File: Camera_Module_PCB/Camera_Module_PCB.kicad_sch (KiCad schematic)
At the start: 66 parts, among them J3 FFC2A32-24-T, SW2 SW_Push, SW3 SW_Push, U2 ESP32-S3R8, U4 MAX98357AETE_T, U5 AP3032KTR-G1, Y1 40MHz

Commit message: Made minor changes to schematic
Schematic is finished except for the inclusion of an RF antenna for Pin 1 of the ESP32. Waiting on team confirmation about its inclusion.
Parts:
- added TP1, TP2, TP3, TP4, TP5, TP6: TestPoint, symbol Connector:TestPoint
- R17: value Riset -> 10
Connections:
- net IR_DIM is gone; now on net LED_CT: U2.37 (SPICLK_P)
- net +3.3V: now also TP4.1
- net GND: now also TP3.1
- net LED_CT: no longer U2.38 (GPIO33)
- net XTAL_N: now also TP6.1
- net at C14.2, L2.1, Y1.1: now also TP5.1
- net at D20.2, U2.50 (U0RXD), U3.3: now also TP2.1; no longer D19.2
- net at U2.49 (U0TXD), U3.4: now also D19.2, TP1.1
- no-connect marks 11 -> 20
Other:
- sheet Power Supply ports: added USB_D+, USB_D-; removed none
- note added: "CAMERA FFC CONNECTOR"
- note added: "LED DRIVER"
- note added: "Place close to VDD CPU & VDD RTC on ESP32"
- note added: "Place close toVDDA1 & 2 on ESP32"
- note removed: "Camera Connector"
- moved on the sheet: C27, C28, C32, C33, C7, C9, D19, D20, D21, D22, D23, J3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

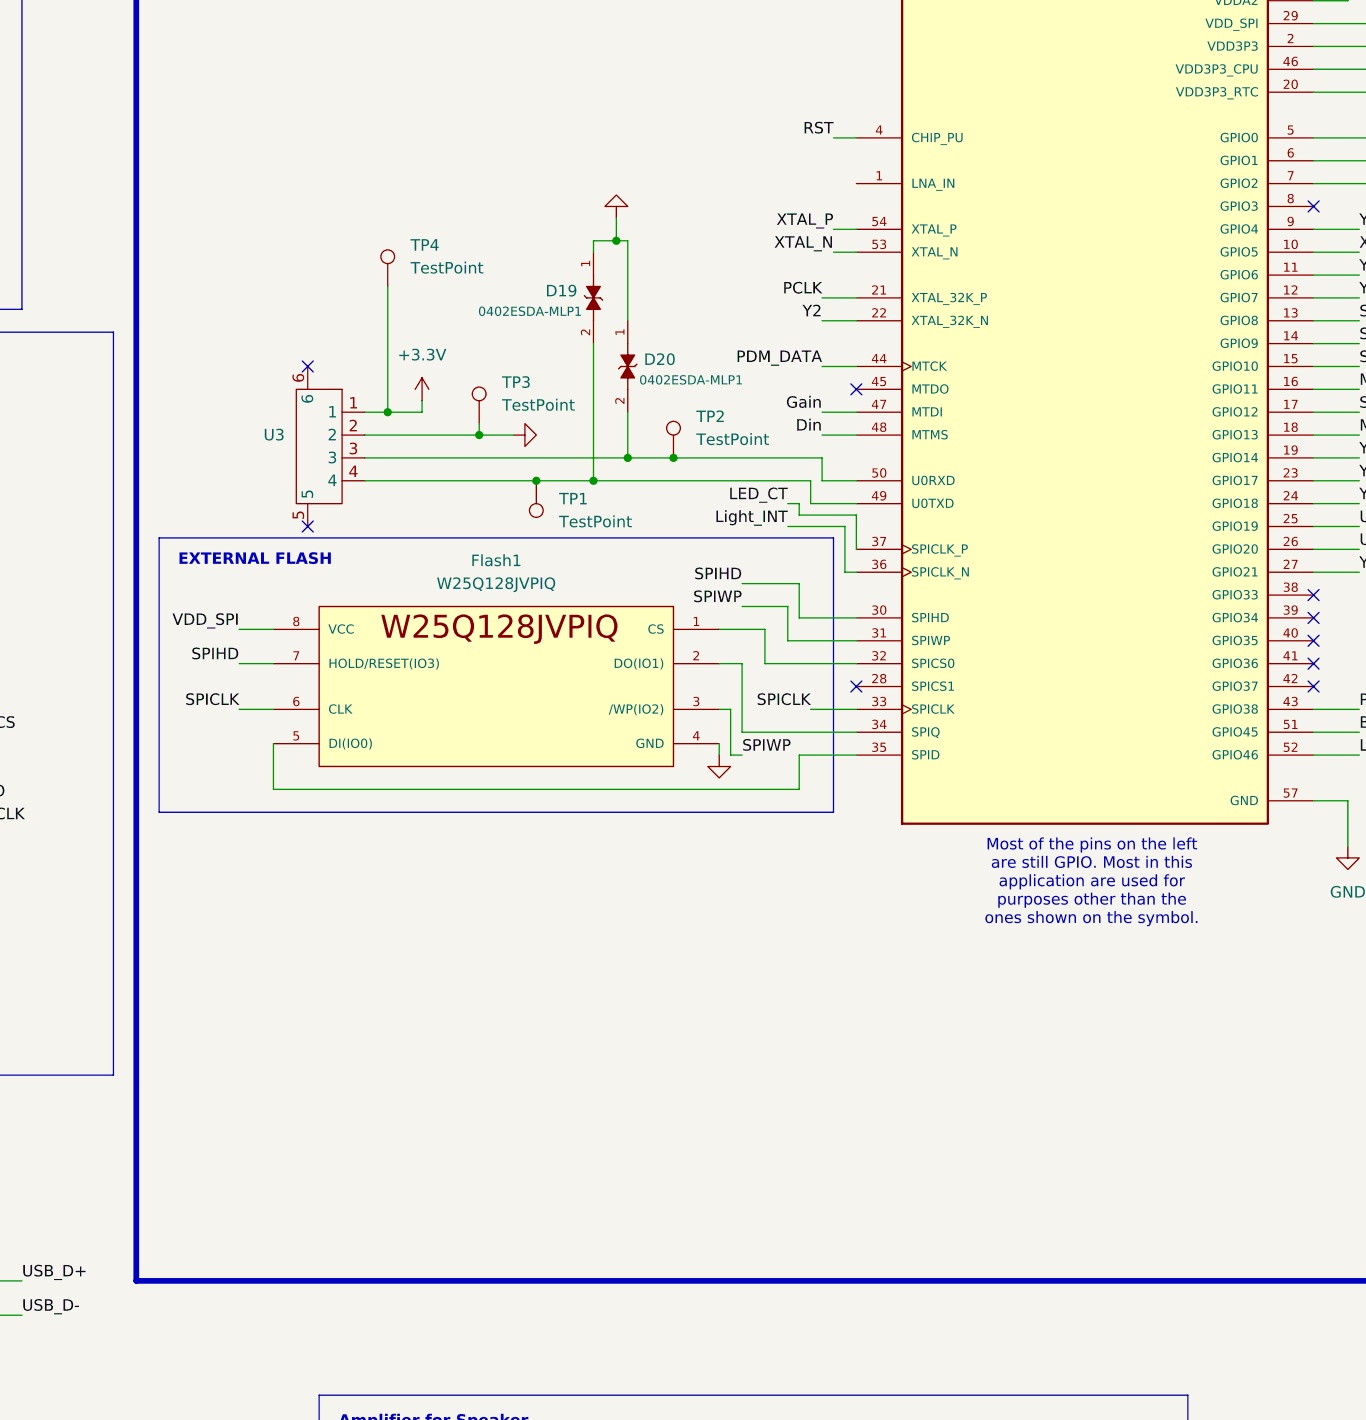
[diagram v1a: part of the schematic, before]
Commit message: Added Most ICs to the General PCB Layout
Most of the intended ICs that are going to be used were put into a general IC layout. A decision will need to be made in regards to the antenna. The ESP32 Model that is being used may be replaced, or remain the same.
Once the decision is made, more can be added.
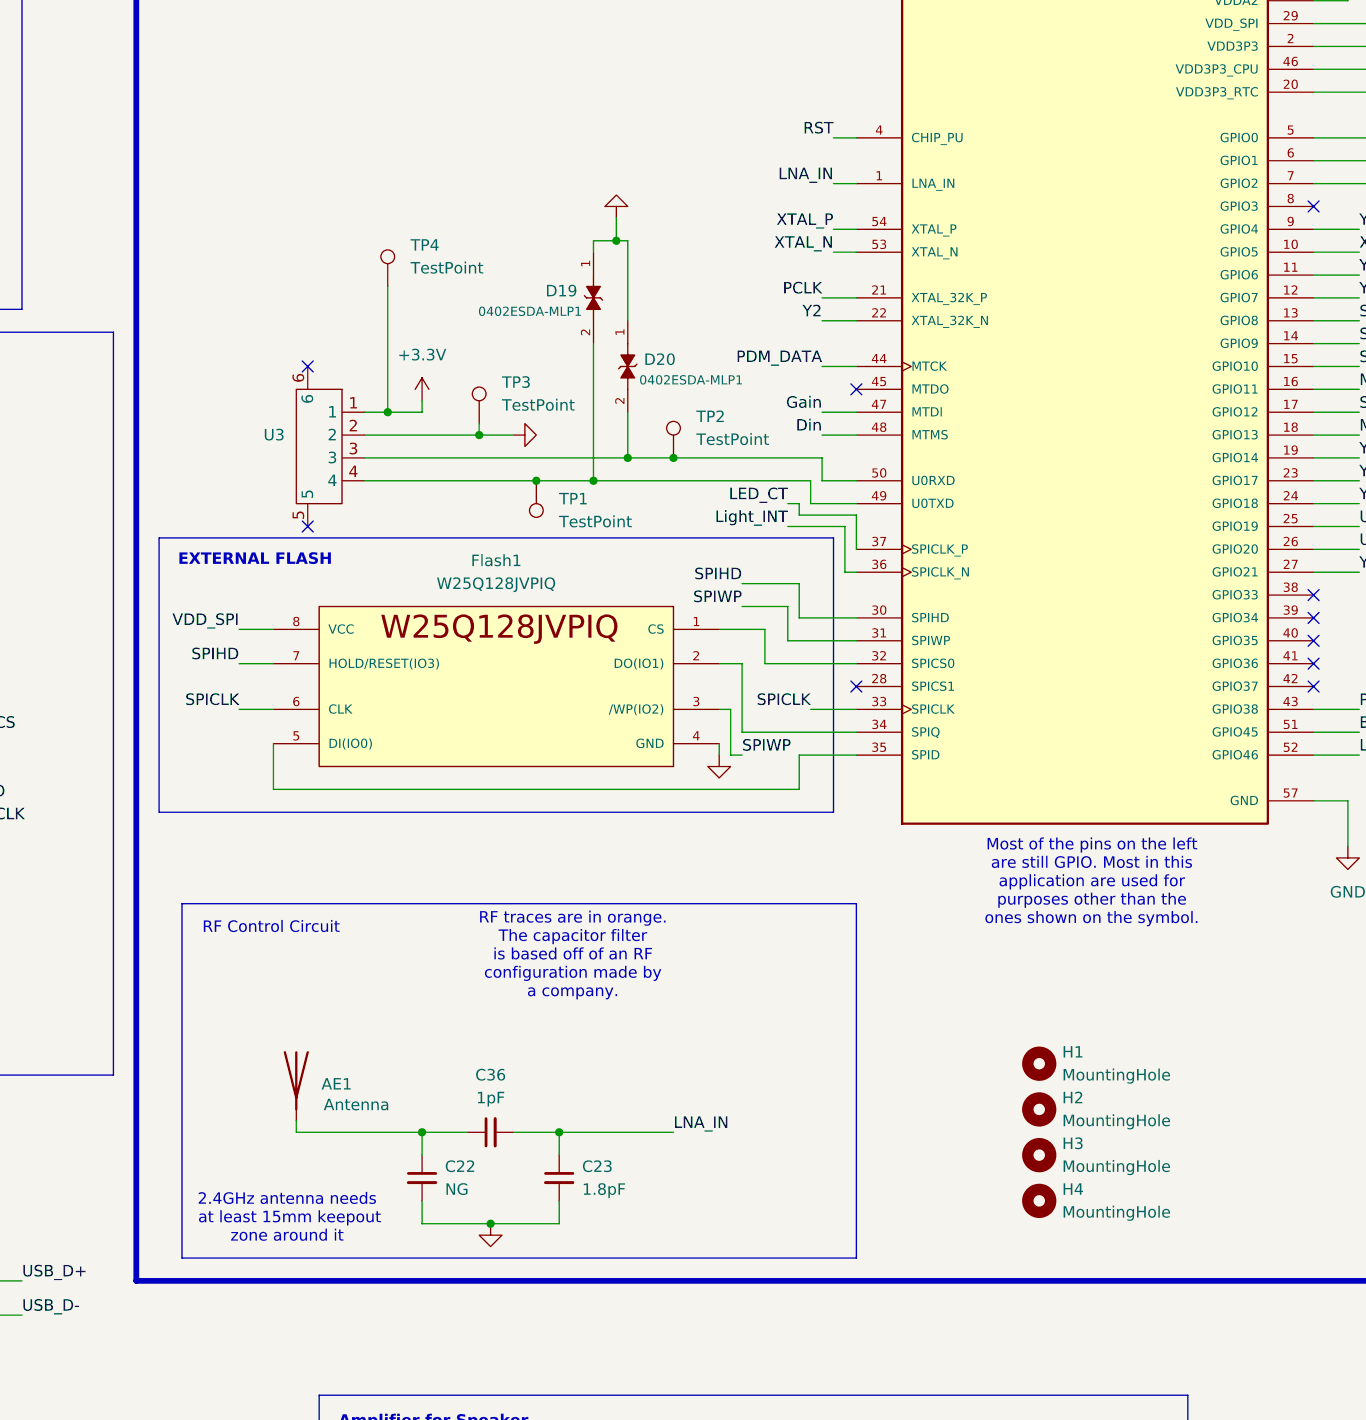
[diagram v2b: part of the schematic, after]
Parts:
- added AE1: Antenna, RF_Antenna:Texas_SWRA117D_2.4GHz_Left, symbol Device:Antenna
- added C22: NG, Capacitor_SMD:C_0603_1608Metric, symbol Device:C_Small
- added C23: 1.8pF, Capacitor_SMD:C_0603_1608Metric, symbol Device:C_Small
- added C36: 1pF, Capacitor_SMD:C_0603_1608Metric, symbol Device:C_Small
- added H1, H2, H3, H4: MountingHole, MountingHole:MountingHole_2.7mm, symbol Mechanical:MountingHole
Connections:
- net GND: now also C22.2, C23.2
- net LNA_IN: now reaches U2.1 (LNA_IN)
- net LNA_IN: now also C23.1, C36.2
- new net: AE1.1 (A), C22.1, C36.1
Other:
- note added: "2.4GHz antenna needs at least 15mm keepout zone around it"
- note added: "RF Control Circuit"
- note added: "RF traces are in orange. The capacitor filter is based off of an RF configuration made by a company."

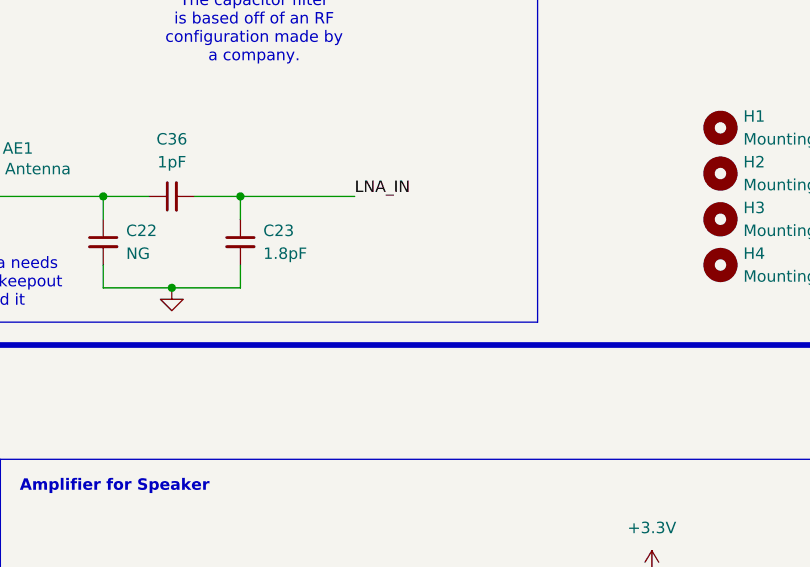
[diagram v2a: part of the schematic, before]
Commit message: MCU Layout Started
The layout for the ESP32 has been started, according to the recommended 4-Layer layout. Please look over the antenna and continue layout.
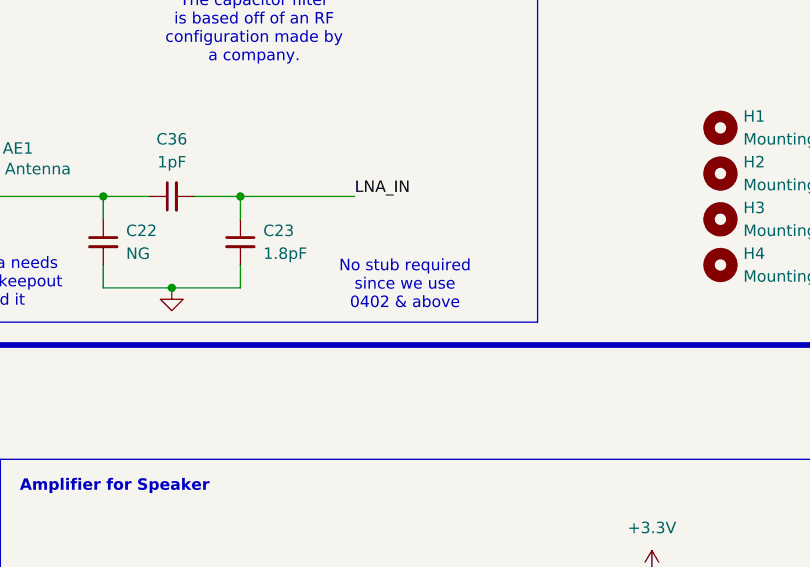
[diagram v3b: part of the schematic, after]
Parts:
- C11, C13, C15, C22, C23, C36, C8: footprint Capacitor_SMD:C_0603_1608Metric -> Capacitor_SMD:C_0402_1005Metric
- L3: footprint Inductor_SMD:L_0603_1608Metric -> Inductor_SMD:L_0402_1005Metric
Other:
- note added: "No stub required since we use 0402 & above"
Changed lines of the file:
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@@
 		)
 	)
+	(text "No stub required\nsince we use \n0402 & above"
+		(exclude_from_sim no)
+		(at 235.458 164.846 0)
+		(effects
+			(font
+				(size 1.27 1.27)
+			)
+		)
+	)
 	(text "EXTERNAL FLASH\n"
 		(exclude_from_sim no)
@@
 			)
 		)
-		(property "Footprint" "Capacitor_SMD:C_0603_1608Metric"
+		(property "Footprint" "Capacitor_SMD:C_0402_1005Metric"
 			(at 363.22 34.29 0)
 			(effects
@@
 			)
 		)
-		(property "Footprint" "Capacitor_SMD:C_0603_1608Metric"
+		(property "Footprint" "Capacitor_SMD:C_0402_1005Metric"
 			(at 340.36 34.29 0)
 			(effects
@@
 			)
 		)
-		(property "Footprint" "Capacitor_SMD:C_0603_1608Metric"
+		(property "Footprint" "Capacitor_SMD:C_0402_1005Metric"
 			(at 209.55 154.94 0)
 			(effects
@@
 			)
 		)
-		(property "Footprint" "Capacitor_SMD:C_0603_1608Metric"
+		(property "Footprint" "Capacitor_SMD:C_0402_1005Metric"
 			(at 384.81 34.29 0)
 			(effects
@@
 			)
 		)
-		(property "Footprint" "Capacitor_SMD:C_0603_1608Metric"
+		(property "Footprint" "Capacitor_SMD:C_0402_1005Metric"
 			(at 201.93 160.02 0)
 			(effects
@@
 			)
 		)
-		(property "Footprint" "Capacitor_SMD:C_0603_1608Metric"
+		(property "Footprint" "Capacitor_SMD:C_0402_1005Metric"
 			(at 217.17 160.02 0)
 			(effects
@@
 			)
 		)
-		(property "Footprint" "Capacitor_SMD:C_0603_1608Metric"
+		(property "Footprint" "Capacitor_SMD:C_0402_1005Metric"
 			(at 351.79 34.29 0)
 			(effects
@@
 			)
 		)
-		(property "Footprint" "Inductor_SMD:L_0603_1608Metric"
+		(property "Footprint" "Inductor_SMD:L_0402_1005Metric"
 			(at 373.38 31.75 0)
 			(effects

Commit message: Made a small comment about LEDs
Made a comment about LEDs. We need to give out LEDs and Diodes a specific part number (usually from Digikey).
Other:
- note added: "Remember to give LEDs a part number corresponding to the color and size we want"
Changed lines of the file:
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@@
+		)
+	)
+	(text "Remember to give\nLEDs a part number\ncorresponding to\nthe color and size we \nwant"
+		(exclude_from_sim no)
+		(at 149.352 256.032 0)
+		(effects
+			(font
+				(size 1.27 1.27)
+			)
 		)
 	)

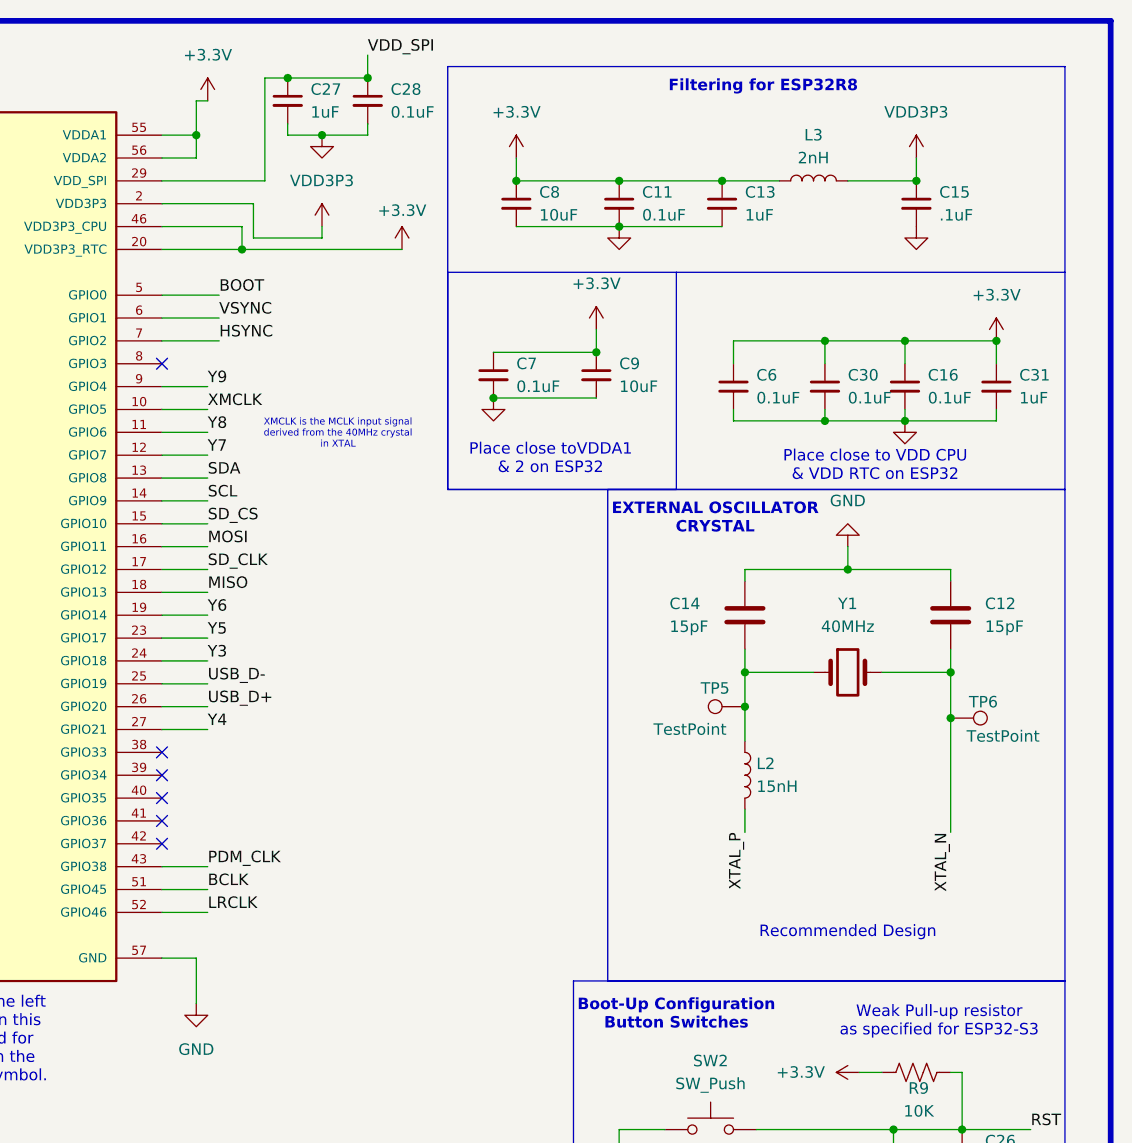
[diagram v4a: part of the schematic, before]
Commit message: Continued to map out ESP32 Module portion of PCB
Continued to follow the Espressif PCB layout by routing power and placing general component location. The quartz crystal footprint was changed and the model we will be using replaced the value of the crystal in the schematic.
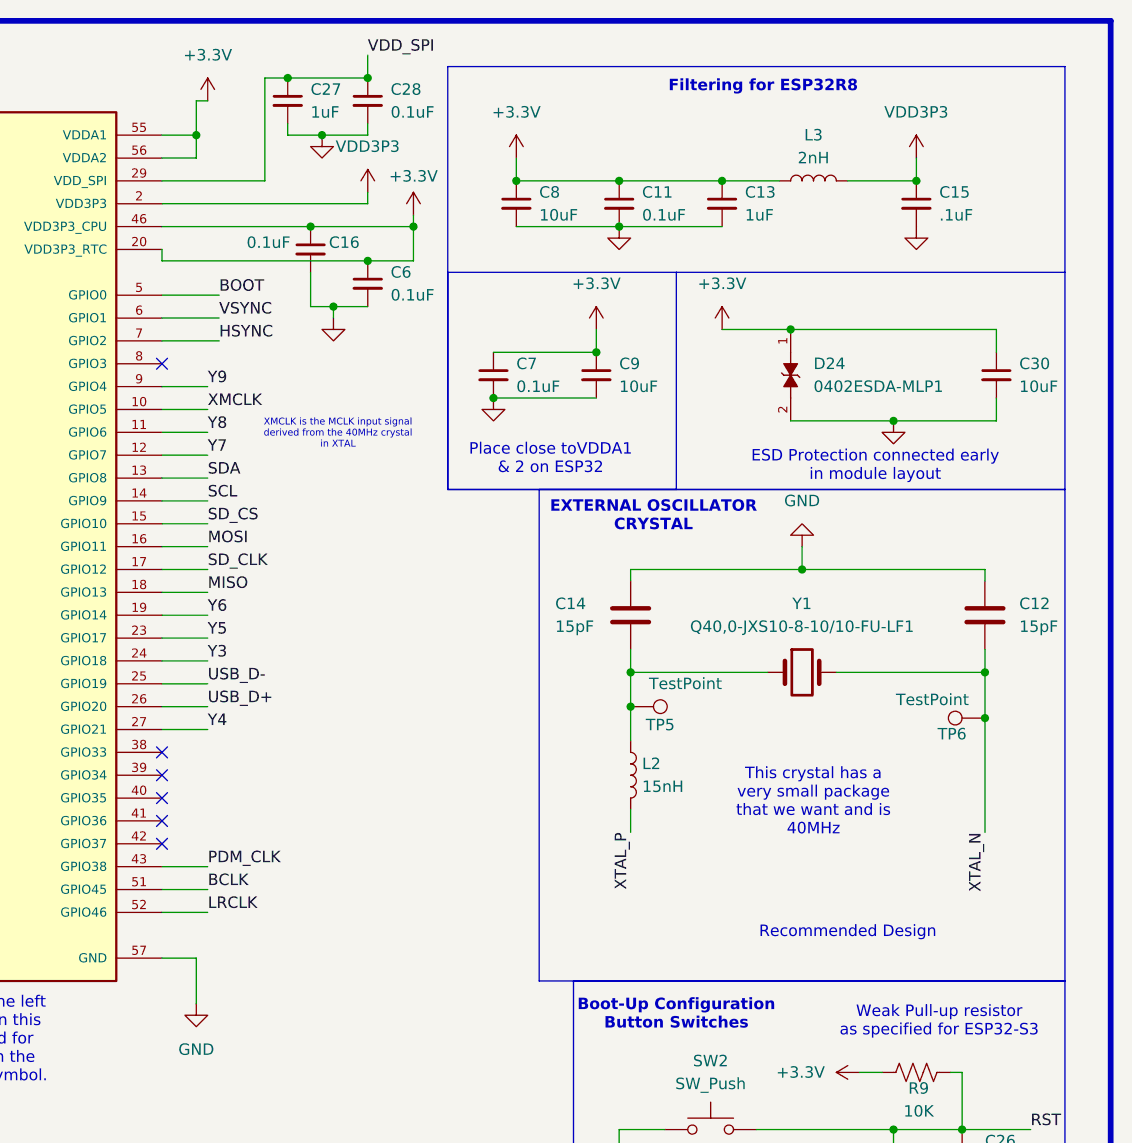
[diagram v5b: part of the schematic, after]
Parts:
- removed C31: 1uF, Capacitor_SMD:C_0603_1608Metric, symbol Device:C_Small
- added D24: 0402ESDA-MLP1, ESP32CAM_Foorprints:ESD_0402ESDA-MLP1, symbol 0402ESDA-MLP1:0402ESDA-MLP1
- C12, C14, C16, C6: footprint Capacitor_SMD:C_0603_1608Metric -> Capacitor_SMD:C_0402_1005Metric
- C30: value 0.1uF -> 10uF; footprint Capacitor_SMD:C_0603_1608Metric -> Capacitor_SMD:C_0402_1005Metric
- L2: footprint Inductor_SMD:L_0603_1608Metric -> Inductor_SMD:L_0402_1005Metric
- Y1: value 40MHz -> Q40,0-JXS10-8-10/10-FU-LF1; footprint Crystal:Crystal_AT310_D3.0mm_L10.0mm_Horizontal -> Crystal:Crystal_SMD_1210-4Pin_1.2x1.0mm
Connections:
- net +3.3V: now also D24.1
- net GND: now also D24.2
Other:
- note added: "ESD Protection connected early in module layout"
- note added: "This crystal has a very small package that we want and is 40MHz"
- note removed: "Place close to VDD CPU & VDD RTC on ESP32"
- moved on the sheet: C12, C14, L2, TP5, TP6, Y1
